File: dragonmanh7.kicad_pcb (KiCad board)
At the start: 4 copper layers, 135.6 x 54.6 mm, 109 parts, among them J1 USB_B, J10 Conn_02x12_Odd_Even, J11 Conn_02x03_Odd_Even, J12 VBAT+, J13 Conn_02x05_Odd_Even, J14 VBATG, J15 Conn_02x02_Odd_Even, J18 Conn_02x05_Odd_Even, J2 73725-0110BLF, J3 RJ45_Amphenol_RJMG1BD3B8K1ANR, J4 Micro_SD_Card, J5 Screw_Terminal_01x06, J6 Conn_02x12_Odd_Even, J7 USB_B, J8 Screw_Terminal_01x02, J9 Conn_02x12_Odd_Even, SW1 RESET, SW2 PC13, U1 STM32H743VITx, U10 USBLC6-2SC6, U11 SN6505, U12 TCAN332, U13 ISL83483, U14 MIC2005A, U2 KSZ8081RNA, U3 ISO1050DUB, U4 ISO3082DW, U5 S25FL127SABMFI101, U6 AP63203, U7 USBLC6-2SC6, U8 STM32F042F6Px, U9 USBLC6-2SC6, Y1 8MHz, Y2 32.768KHz, Y3 25MHz

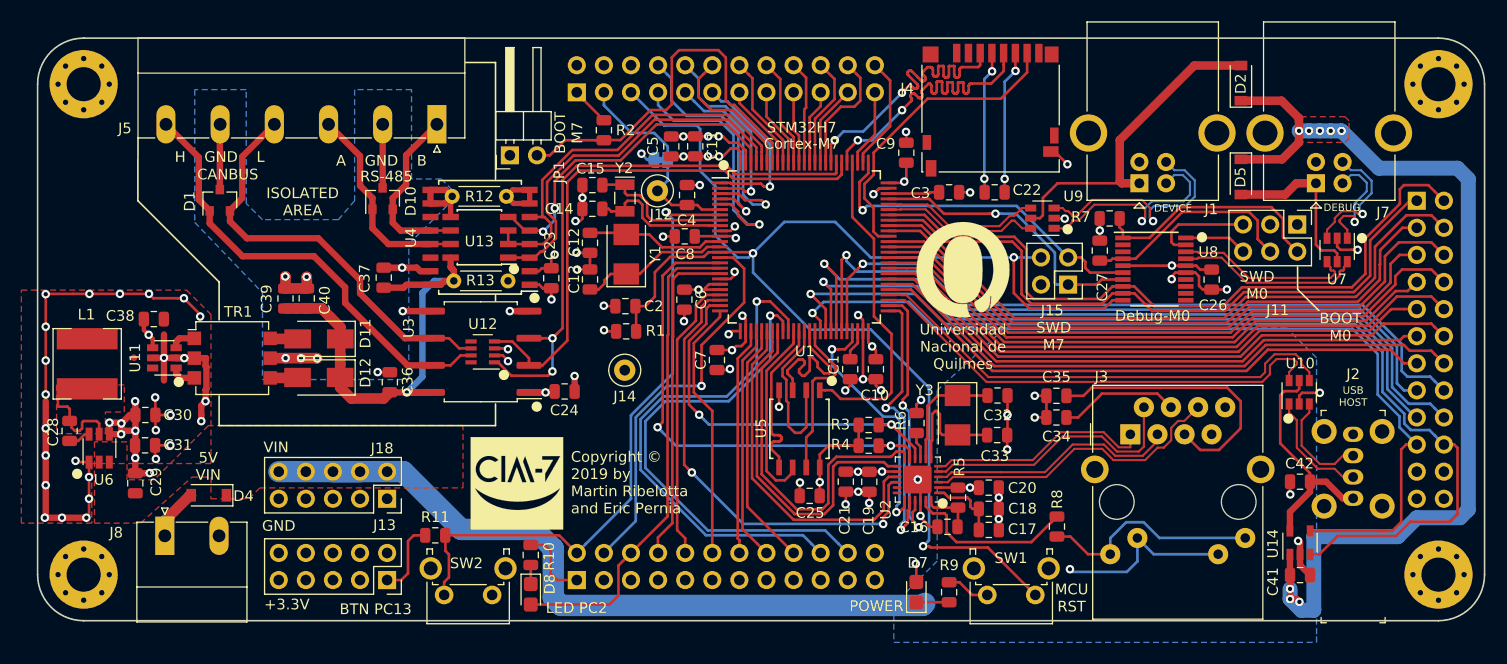
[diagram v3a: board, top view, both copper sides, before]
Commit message: Clear schematic library table and minor pcb footprint capacitor reorganization
Signed-off-by: Martin Ribelotta <martinribelotta@gmail.com>
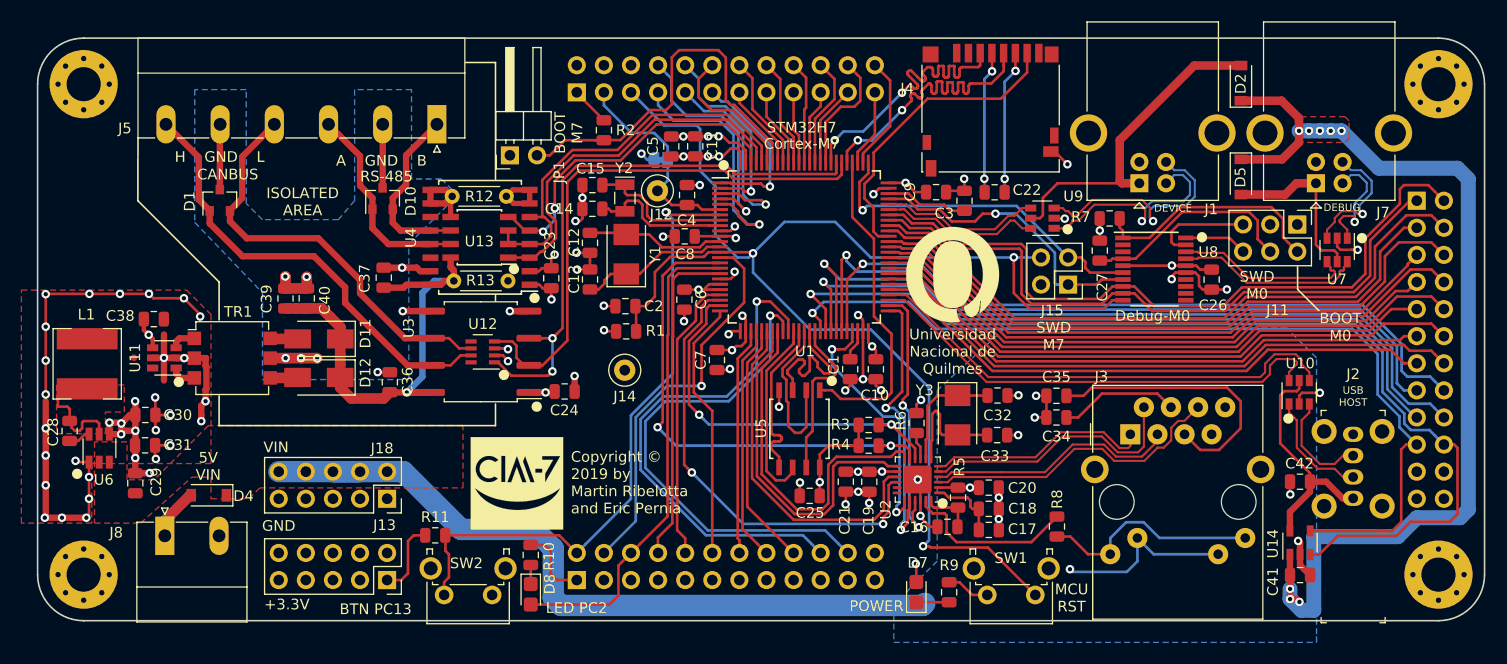
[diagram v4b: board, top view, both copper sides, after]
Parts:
- moved C9 4.63 mm to (142.9, 42.4), turned to 0 degrees
- moved C3 1.65 mm to (145.6, 43.2), turned to 90 degrees
- moved LOGO2 1.08 mm to (144.4, 50.2)
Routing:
- net Net-(C3-Pad1): track 4.79 -> 7.78 mm
- net GND: track 170.6 -> 168.4 mm, vias 60 -> 59
- net /PC6: track 56.9 -> 55.9 mm
- net /SWDIO: track 27.1 -> 27.7 mm
- net +3V3: track 160.3 -> 160.8 mm

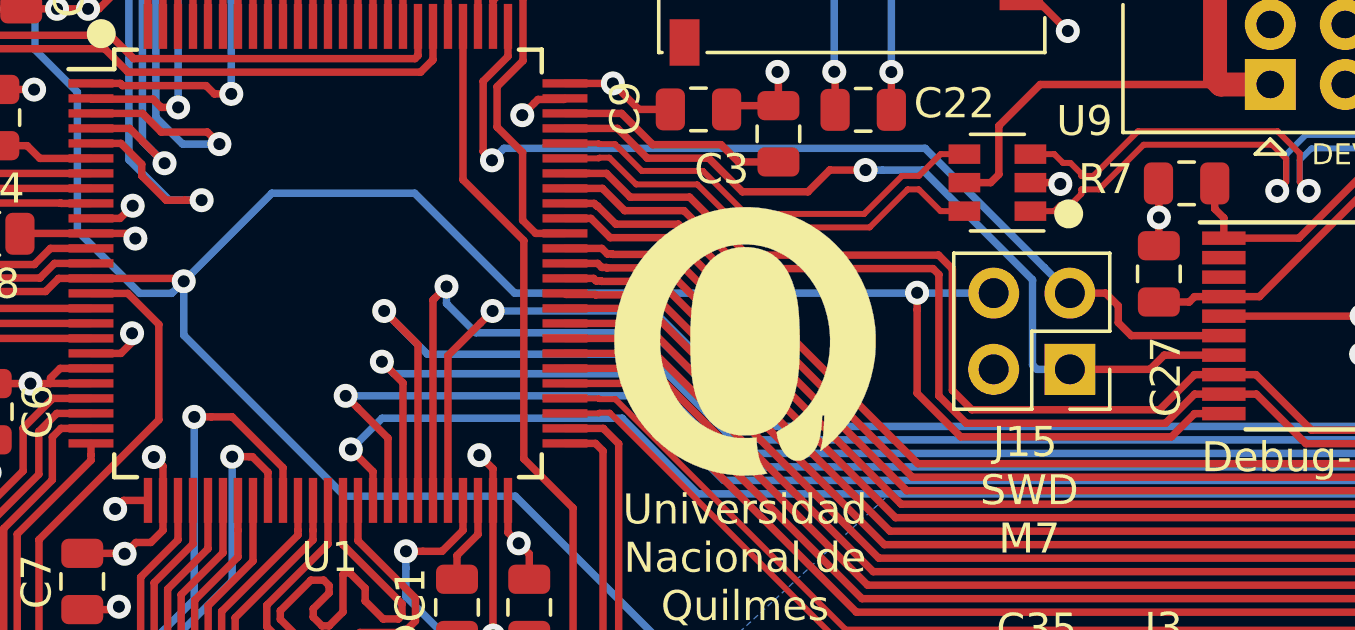
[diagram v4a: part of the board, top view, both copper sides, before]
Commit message: Improve reset tracesu
Signed-off-by: Martin Ribelotta <martinribelotta@gmail.com>
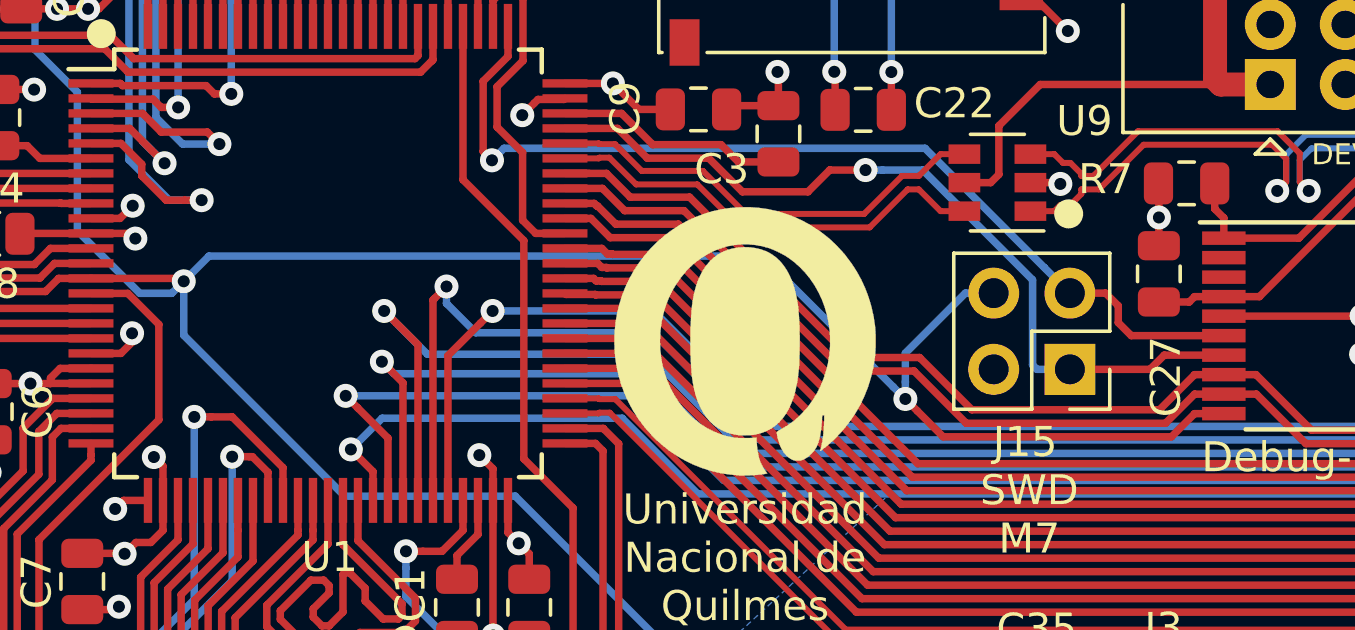
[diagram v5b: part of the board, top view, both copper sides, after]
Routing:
- net /U1_RX: track 67.0 -> 64.6 mm
- net /U1_TX: track 62.4 -> 60.1 mm
- net /~RESET: track 134.3 -> 133.3 mm
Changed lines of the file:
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@@
     (thickness 1.6)
     (drawings 76)
-    (tracks 2297)
+    (tracks 2296)
     (zones 0)
     (modules 109)
@@
   (segment (start 117.965511 48.447669) (end 121.129001 48.447669) (width 0.25) (layer F.Cu) (net 33))
   (segment (start 121.129001 48.447669) (end 121.566529 48.010141) (width 0.25) (layer F.Cu) (net 33))
-  (segment (start 128.67386 45.17136) (end 125.73762 48.1076) (width 0.25) (layer B.Cu) (net 33))
-  (segment (start 152.73528 48.5013) (end 136.7663 48.5013) (width 0.25) (layer B.Cu) (net 33))
-  (segment (start 133.43636 45.17136) (end 128.67386 45.17136) (width 0.25) (layer B.Cu) (net 33))
-  (segment (start 136.7663 48.5013) (end 133.43636 45.17136) (width 0.25) (layer B.Cu) (net 33))
   (segment (start 117.407711 36.127711) (end 114.3 33.02) (width 0.25) (layer B.Cu) (net 33))
   (segment (start 120.77954 36.45916) (end 120.448091 36.127711) (width 0.25) (layer B.Cu) (net 33))
@@
   (segment (start 131.1021 55.2704) (end 136.7917 55.2704) (width 0.25) (layer B.Cu) (net 33))
   (segment (start 125.73762 49.90592) (end 131.1021 55.2704) (width 0.25) (layer B.Cu) (net 33))
-  (via (at 150.183579 48.4886) (size 0.8) (drill 0.4) (layers F.Cu B.Cu) (net 33))
-  (segment (start 158.66186 53.2892) (end 151.635178 53.2892) (width 0.25) (layer F.Cu) (net 33))
-  (segment (start 150.183579 51.837601) (end 150.183579 49.054285) (width 0.25) (layer F.Cu) (net 33))
-  (segment (start 159.43256 52.5185) (end 158.66186 53.2892) (width 0.25) (layer F.Cu) (net 33))
+  (via (at 149.79142 52.02936) (size 0.8) (drill 0.4) (layers F.Cu B.Cu) (net 33))
+  (segment (start 151.05126 53.2892) (end 150.191419 52.429359) (width 0.25) (layer F.Cu) (net 33))
+  (segment (start 150.191419 52.429359) (end 149.79142 52.02936) (width 0.25) (layer F.Cu) (net 33))
+  (segment (start 158.66186 53.2892) (end 151.05126 53.2892) (width 0.25) (layer F.Cu) (net 33))
   (segment (start 160.40756 52.5185) (end 159.43256 52.5185) (width 0.25) (layer F.Cu) (net 33))
-  (segment (start 150.183579 49.054285) (end 150.183579 48.4886) (width 0.25) (layer F.Cu) (net 33))
-  (segment (start 151.635178 53.2892) (end 150.183579 51.837601) (width 0.25) (layer F.Cu) (net 33))
+  (segment (start 159.43256 52.5185) (end 158.66186 53.2892) (width 0.25) (layer F.Cu) (net 33))
+  (segment (start 149.391421 51.629361) (end 149.79142 52.02936) (width 0.25) (layer B.Cu) (net 33))
+  (segment (start 145.02892 47.26686) (end 149.391421 51.629361) (width 0.25) (layer B.Cu) (net 33))
+  (segment (start 125.73762 48.1076) (end 126.57836 47.26686) (width 0.25) (layer B.Cu) (net 33))
+  (segment (start 126.57836 47.26686) (end 145.02892 47.26686) (width 0.25) (layer B.Cu) (net 33))
+  (segment (start 149.79142 51.463675) (end 149.79142 52.02936) (width 0.25) (layer B.Cu) (net 33))
+  (segment (start 149.79142 50.50282) (end 149.79142 51.463675) (width 0.25) (layer B.Cu) (net 33))
+  (segment (start 152.73528 48.5013) (end 151.79294 48.5013) (width 0.25) (layer B.Cu) (net 33))
+  (segment (start 151.79294 48.5013) (end 149.79142 50.50282) (width 0.25) (layer B.Cu) (net 33))
   (segment (start 130.19532 64.94018) (end 130.72364 64.41186) (width 0.25) (layer F.Cu) (net 34))
   (segment (start 129.667 64.94018) (end 130.19532 64.94018) (width 0.25) (layer F.Cu) (net 34))
@@
   (segment (start 163.143501 53.518512) (end 169.984557 53.518512) (width 0.25) (layer F.Cu) (net 40))
   (segment (start 187.30355 43.18) (end 187.96 43.18) (width 0.25) (layer F.Cu) (net 40))
+  (segment (start 139.693105 45.010141) (end 140.43542 45.752457) (width 0.25) (layer F.Cu) (net 40))
+  (segment (start 147.758439 51.097611) (end 150.080001 51.097611) (width 0.25) (layer F.Cu) (net 40))
+  (segment (start 150.080001 51.097611) (end 151.821578 52.839189) (width 0.25) (layer F.Cu) (net 40))
   (segment (start 151.821578 52.839189) (end 158.461871 52.839189) (width 0.25) (layer F.Cu) (net 40))
-  (segment (start 140.43542 45.752457) (end 142.413286 45.752457) (width 0.25) (layer F.Cu) (net 40))
-  (segment (start 158.461871 52.839189) (end 159.43256 51.8685) (width 0.25) (layer F.Cu) (net 40))
-  (segment (start 142.413286 45.752457) (end 144.344679 47.683851) (width 0.25) (layer F.Cu) (net 40))
-  (segment (start 144.344679 47.683851) (end 150.712456 47.683851) (width 0.25) (layer F.Cu) (net 40))
   (segment (start 159.43256 51.8685) (end 160.40756 51.8685) (width 0.25) (layer F.Cu) (net 40))
-  (segment (start 150.908589 51.9262) (end 151.821578 52.839189) (width 0.25) (layer F.Cu) (net 40))
+  (segment (start 158.461871 52.839189) (end 159.43256 51.8685) (width 0.25) (layer F.Cu) (net 40))
+  (segment (start 142.413286 45.752457) (end 147.758439 51.097611) (width 0.25) (layer F.Cu) (net 40))
   (segment (start 138.445281 45.010141) (end 139.693105 45.010141) (width 0.25) (layer F.Cu) (net 40))
-  (segment (start 139.693105 45.010141) (end 140.43542 45.752457) (width 0.25) (layer F.Cu) (net 40))
-  (segment (start 150.712456 47.683851) (end 150.908589 47.879984) (width 0.25) (layer F.Cu) (net 40))
-  (segment (start 150.908589 47.879984) (end 150.908589 51.9262) (width 0.25) (layer F.Cu) (net 40))
+  (segment (start 140.43542 45.752457) (end 142.413286 45.752457) (width 0.25) (layer F.Cu) (net 40))
   (segment (start 189.0395 41.7195) (end 189.650001 42.330001) (width 0.25) (layer F.Cu) (net 41))
   (segment (start 186.36996 42.1005) (end 186.75096 41.7195) (width 0.25) (layer F.Cu) (net 41))
@@
   (segment (start 169.798157 53.068501) (end 171.5668 51.299857) (width 0.25) (layer F.Cu) (net 41))
   (segment (start 183.138649 50.033351) (end 183.138649 46.70849) (width 0.25) (layer F.Cu) (net 41))
+  (segment (start 140.62182 45.302446) (end 139.829515 44.510141) (width 0.25) (layer F.Cu) (net 41))
   (segment (start 139.829515 44.510141) (end 139.244521 44.510141) (width 0.25) (layer F.Cu) (net 41))
-  (segment (start 142.599685 45.302446) (end 140.62182 45.302446) (width 0.25) (layer F.Cu) (net 41))
-  (segment (start 144.531079 47.23384) (end 142.599685 45.302446) (width 0.25) (layer F.Cu) (net 41))
+  (segment (start 152.007978 52.389178) (end 150.2664 50.6476) (width 0.25) (layer F.Cu) (net 41))
   (segment (start 160.40756 51.2185) (end 159.43256 51.2185) (width 0.25) (layer F.Cu) (net 41))
-  (segment (start 151.3586 47.693584) (end 150.898856 47.23384) (width 0.25) (layer F.Cu) (net 41))
-  (segment (start 150.898856 47.23384) (end 144.531079 47.23384) (width 0.25) (layer F.Cu) (net 41))
-  (segment (start 152.007978 52.389178) (end 151.3586 51.7398) (width 0.25) (layer F.Cu) (net 41))
-  (segment (start 151.3586 51.7398) (end 151.3586 47.693584) (width 0.25) (layer F.Cu) (net 41))
   (segment (start 159.43256 51.2185) (end 158.261882 52.389178) (width 0.25) (layer F.Cu) (net 41))
-  (segment (start 139.244521 44.510141) (end 138.445281 44.510141) (width 0.25) (layer F.Cu) (net 41))
-  (segment (start 140.62182 45.302446) (end 139.829515 44.510141) (width 0.25) (layer F.Cu) (net 41))
+  (segment (start 142.599685 45.302446) (end 140.62182 45.302446) (width 0.25) (layer F.Cu) (net 41))
   (segment (start 158.261882 52.389178) (end 152.007978 52.389178) (width 0.25) (layer F.Cu) (net 41))
+  (segment (start 139.244521 44.510141) (end 138.445281 44.510141) (width 0.25) (layer F.Cu) (net 41))
+  (segment (start 150.2664 50.6476) (end 147.944839 50.6476) (width 0.25) (layer F.Cu) (net 41))
+  (segment (start 147.944839 50.6476) (end 142.599685 45.302446) (width 0.25) (layer F.Cu) (net 41))
   (segment (start 180.26994 49.82772) (end 180.26994 50.038497) (width 0.2) (layer F.Cu) (net 42))
   (segment (start 179.54494 49.10272) (end 179.869939 49.427719) (width 0.2) (layer F.Cu) (net 42))

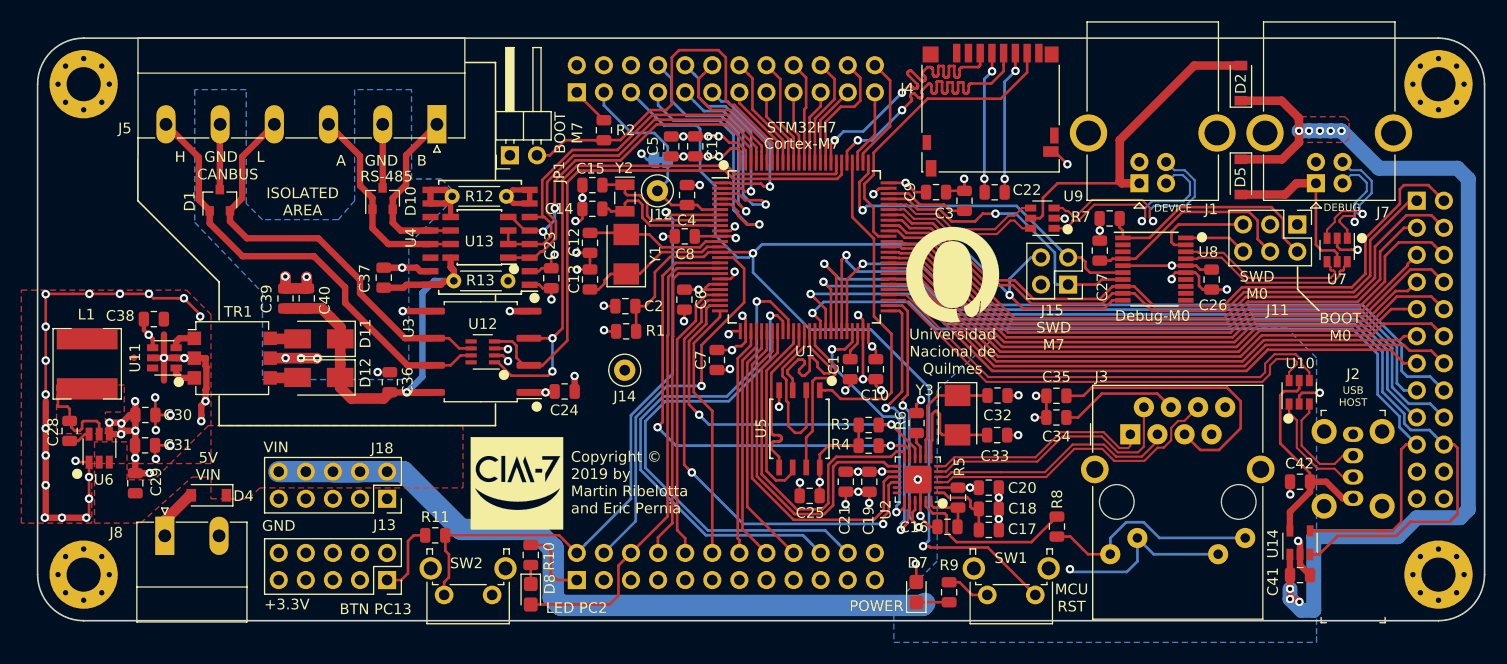
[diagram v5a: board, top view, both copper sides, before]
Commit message: Add rs485/CANBUS optional termination footprints
Signed-off-by: Martin Ribelotta <martinribelotta@gmail.com>
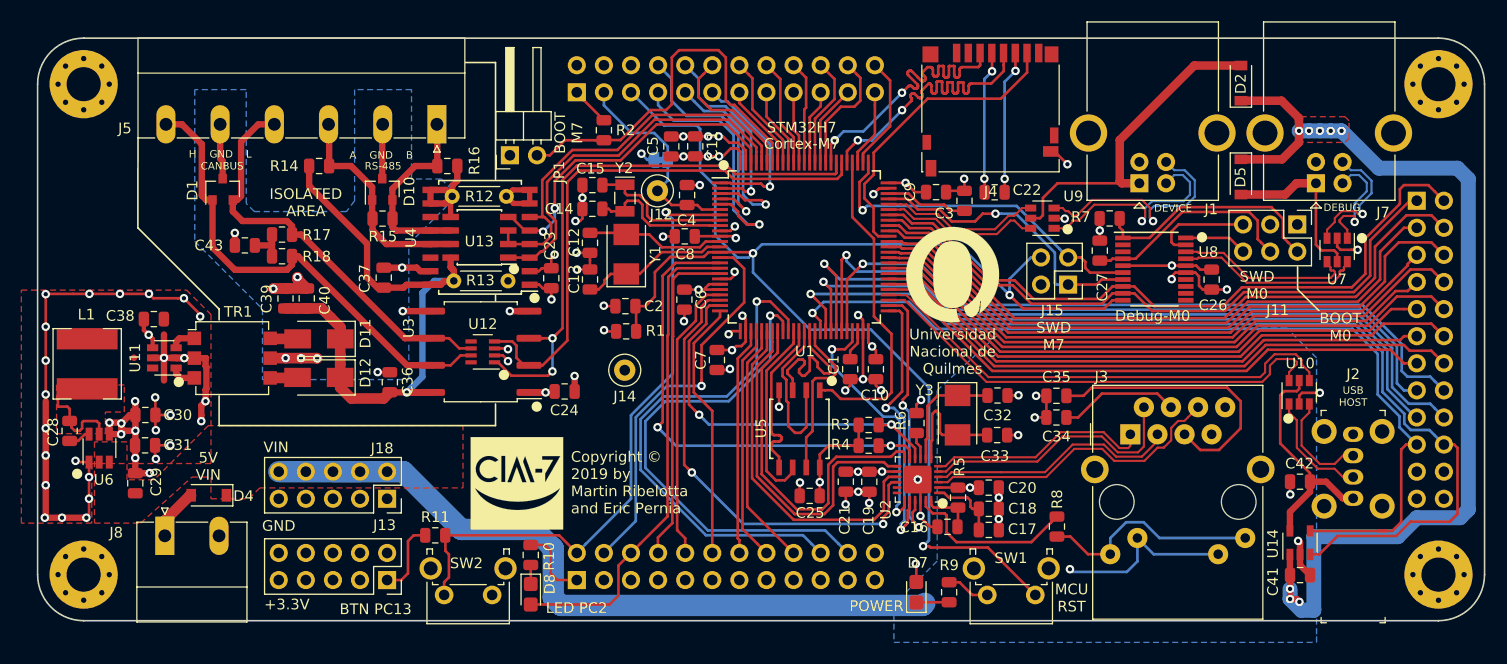
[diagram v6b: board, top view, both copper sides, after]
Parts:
- added C43: 10p, Capacitor_SMD:C_0805_2012Metric, F.Cu at (78.1, 47.4)
- added R14: 2K2, Resistor_SMD:R_0805_2012Metric, F.Cu at (85.1, 39.9)
- added R15: 120R, Resistor_SMD:R_0805_2012Metric, F.Cu at (91.0, 44.9)
- added R16: 2K2, Resistor_SMD:R_0805_2012Metric, F.Cu at (97.1, 39.9)
- added R17: 60R, Resistor_SMD:R_0805_2012Metric, F.Cu at (81.6, 46.4)
- added R18: 60R, Resistor_SMD:R_0805_2012Metric, F.Cu at (81.6, 48.4)
- moved D1 1.06 mm to (76.0, 42.1)
- moved D10 0.87 mm to (91.0, 42.1)
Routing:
- net +5P: track 46.6 -> 61.3 mm
- net Net-(C43-Pad1): track 0.00 -> 3.68 mm
- net /CAN_H: track 42.2 -> 45.3 mm
- net GNDPWR: track 37.0 -> 39.8 mm, vias 8 -> 9
- net /RS485_A: track 16.7 -> 18.2 mm
- net /RS485_B: track 19.4 -> 20.7 mm
